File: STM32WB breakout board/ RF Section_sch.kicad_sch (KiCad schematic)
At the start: 15 parts, among them J3 RSP-122811-02, U2 AMS1117-3.3

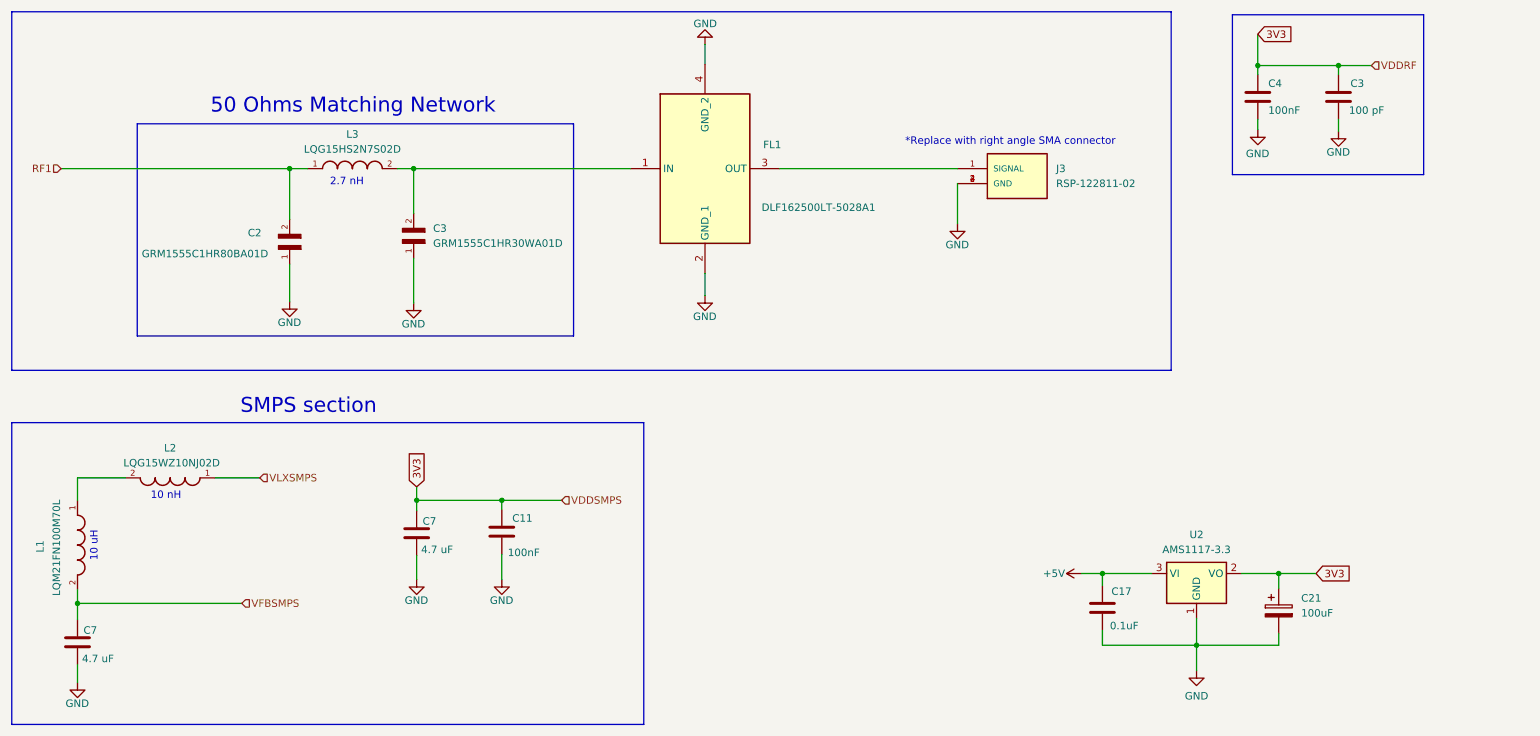
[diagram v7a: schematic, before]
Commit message: USB added
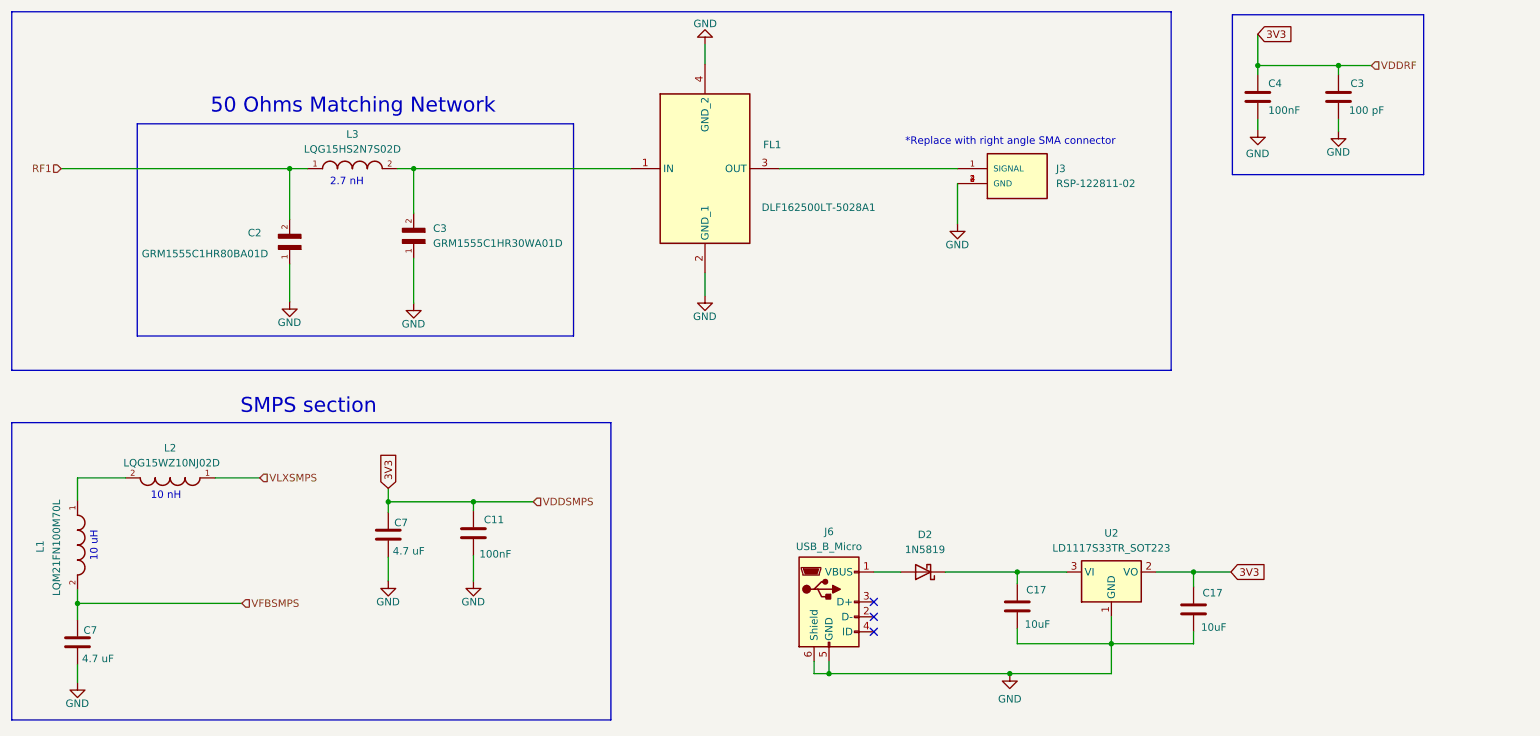
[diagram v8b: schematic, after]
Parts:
- removed C17: 0.1uF, Capacitor_THT:C_Disc_D6.0mm_W2.5mm_P5.00mm, symbol Device:C
- removed C21: 100uF, Capacitor_THT:CP_Radial_D8.0mm_P3.50mm, symbol Device:C_Polarized
- removed U2: AMS1117-3.3, Package_TO_SOT_SMD:SOT-223-3_TabPin2, symbol Regulator_Linear:AMS1117-3.3
- added C17 (x2): 10uF, Capacitor_THT:CP_Radial_D4.0mm_P2.00mm, symbol Device:C
- added D2: 1N5819, Diode_THT:D_DO-41_SOD81_P10.16mm_Horizontal, symbol Diode:1N5819
- added J6: USB_B_Micro, Connector_USB:USB_Micro-B_Amphenol_10103594-0001LF_Horizontal, symbol Connector:USB_B_Micro
- added U2: LD1117S33TR_SOT223, Package_TO_SOT_SMD:SOT-223-3_TabPin2, symbol Regulator_Linear:LD1117S33TR_SOT223
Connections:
- net 3V3: now also C17.1, U2.2 (VO)
- net GND: now also C17.2, C17.2, J6.5 (GND), J6.6 (Shield), U2.1 (GND)
- new net: C17.1, D2.1 (K), U2.3 (VI)
- new net: D2.2 (A), J6.1 (VBUS)
- no-connect marks 0 -> 3
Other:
- moved on the sheet: C11, C7
